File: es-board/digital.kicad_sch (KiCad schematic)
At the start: 25 parts, among them J1 Conn_02x02_Odd_Even, Q5 IRF530NSTRLPB, SW1 SW_SPST, SW2 SW_SPST, SW3 SW_SPST, SW4 SW_SPST, SW5 SW_SPST, U2 ATmega32U4-A, U5 OLED, Y1 16MHz Crystal

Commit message: Added BOM
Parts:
- C1, C4, C5: DPN (none) -> 1276-3091-1-ND; MPN (none) -> CL31B105KBHNFNE
- C2, C3: value 18p -> 24p; DPN (none) -> 478-12061A240JAT2ACT-ND; MPN (none) -> 12061A240JAT2A
- C6, C7: DPN (none) -> 1276-1017-1-ND; MPN (none) -> CL31B104KBCNNNC
- D1: DPN (none) -> 160-1169-1-ND; MPN (none) -> LTST-C150GKT
- D2: DPN (none) -> 160-1403-1-ND; MPN (none) -> LTST-C150KFKT
- J1: value Conn_02x02_Odd_Even -> DNP
- R1: DPN (none) -> RMCF1206JG100K; MPN (none) -> RMCF1206JG100K
- R14, R6: DPN (none) -> 738-RMCF1206JG10K0CT-ND; MPN (none) -> RMCF1206JG10K0
- R7, R8: DPN (none) -> RMCF1206JT1K00CT-ND; MPN (none) -> RMCF1206JT1K00
- SW1, SW2, SW3, SW4, SW5: footprint Button_Switch_SMD:SW_Push_1P1T_NO_6x6mm_H9.5mm -> Button_Switch_SMD:SW_SPST_SKQG_WithStem; DPN (none) -> CKN12220-1-ND; MPN (none) -> PTS526 SM15 SMTR2 LFS
- U2: DPN (none) -> ATMEGA32U4-AURCT-ND; MPN (none) -> IC MCU 8BIT 32KB FLASH 44TQFP
- U5: DPN (none) -> 1528-1512-ND; MPN (none) -> 938
- Y1: DPN (none) -> 2151-RH100-16.000-16-3030-EXT-TRCT-ND; MPN (none) -> RH100-16.000-16-3030-EXT-TR
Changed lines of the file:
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@@
+      (effects (font (size 1.27 1.27)) hide)
+    )
+    (property "DPN" "2151-RH100-16.000-16-3030-EXT-TRCT-ND" (at 47.625 66.04 0)
+      (effects (font (size 1.27 1.27)) hide)
+    )
+    (property "MPN" "RH100-16.000-16-3030-EXT-TR" (at 47.625 66.04 0)
       (effects (font (size 1.27 1.27)) hide)
     )
@@
       (effects (font (size 1.27 1.27)) hide)
     )
+    (property "DPN" "160-1169-1-ND" (at 34.925 129.54 0)
+      (effects (font (size 1.27 1.27)) hide)
+    )
+    (property "MPN" "LTST-C150GKT" (at 34.925 129.54 0)
+      (effects (font (size 1.27 1.27)) hide)
+    )
     (pin "1")
     (pin "2")
@@
       (effects (font (size 1.27 1.27)))
     )
-    (property "Value" "18p" (at 34.925 66.04 90)
+    (property "Value" "24p" (at 34.925 66.04 90)
       (effects (font (size 1.27 1.27)))
     )
@@
       (effects (font (size 1.27 1.27)) hide)
     )
+    (property "DPN" "478-12061A240JAT2ACT-ND" (at 34.925 69.85 0)
+      (effects (font (size 1.27 1.27)) hide)
+    )
+    (property "MPN" "12061A240JAT2A" (at 34.925 69.85 0)
+      (effects (font (size 1.27 1.27)) hide)
+    )
     (pin "1")
     (pin "2")
@@
       (effects (font (size 1.27 1.27)))
     )
-    (property "Footprint" "Button_Switch_SMD:SW_Push_1P1T_NO_6x6mm_H9.5mm" (at 226.06 109.22 0)
+    (property "Footprint" "Button_Switch_SMD:SW_SPST_SKQG_WithStem" (at 226.06 109.22 0)
       (effects (font (size 1.27 1.27)) hide)
     )
     (property "Datasheet" "~" (at 226.06 109.22 0)
+      (effects (font (size 1.27 1.27)) hide)
+    )
+    (property "DPN" "CKN12220-1-ND" (at 226.06 109.22 0)
+      (effects (font (size 1.27 1.27)) hide)
+    )
+    (property "MPN" "PTS526 SM15 SMTR2 LFS" (at 226.06 109.22 0)
       (effects (font (size 1.27 1.27)) hide)
     )
@@
       (effects (font (size 1.27 1.27)))
     )
-    (property "Footprint" "Button_Switch_SMD:SW_Push_1P1T_NO_6x6mm_H9.5mm" (at 45.085 58.42 0)
+    (property "Footprint" "Button_Switch_SMD:SW_SPST_SKQG_WithStem" (at 45.085 58.42 0)
       (effects (font (size 1.27 1.27)) hide)
     )
@@
       (effects (font (size 1.27 1.27)) hide)
     )
+    (property "DPN" "CKN12220-1-ND" (at 45.085 58.42 0)
+      (effects (font (size 1.27 1.27)) hide)
+    )
+    (property "MPN" "PTS526 SM15 SMTR2 LFS" (at 45.085 58.42 0)
+      (effects (font (size 1.27 1.27)) hide)
+    )
     (pin "1")
     (pin "2")
@@
     )
     (property "Datasheet" "~" (at 31.115 96.52 0)
+      (effects (font (size 1.27 1.27)) hide)
+    )
+    (property "DPN" "1276-1017-1-ND" (at 31.115 96.52 0)
+      (effects (font (size 1.27 1.27)) hide)
+    )
+    (property "MPN" "CL31B104KBCNNNC" (at 31.115 96.52 0)
       (effects (font (size 1.27 1.27)) hide)
     )
@@
     )
     (property "Datasheet" "~" (at 213.995 66.675 0)
+      (effects (font (size 1.27 1.27)) hide)
+    )
+    (property "DPN" "738-RMCF1206JG10K0CT-ND" (at 213.995 66.675 0)
+      (effects (font (size 1.27 1.27)) hide)
+    )
+    (property "MPN" "RMCF1206JG10K0" (at 213.995 66.675 0)
       (effects (font (size 1.27 1.27)) hide)
     )
@@
       (effects (font (size 1.27 1.27)) hide)
     )
+    (property "DPN" "RMCF1206JG100K" (at 61.595 54.61 0)
+      (effects (font (size 1.27 1.27)) hide)
+    )
+    (property "MPN" "RMCF1206JG100K" (at 61.595 54.61 0)
+      (effects (font (size 1.27 1.27)) hide)
+    )
     (pin "1")
     (pin "2")
@@
       (effects (font (size 1.27 1.27)) hide)
     )
+    (property "DPN" "1276-3091-1-ND" (at 53.975 54.61 0)
+      (effects (font (size 1.27 1.27)) hide)
+    )
+    (property "MPN" "CL31B105KBHNFNE" (at 53.975 54.61 0)
+      (effects (font (size 1.27 1.27)) hide)
+    )
     (pin "1")
     (pin "2")
@@
       (effects (font (size 1.27 1.27)))
     )
-    (property "Footprint" "Button_Switch_SMD:SW_Push_1P1T_NO_6x6mm_H9.5mm" (at 226.06 116.84 0)
+    (property "Footprint" "Button_Switch_SMD:SW_SPST_SKQG_WithStem" (at 226.06 116.84 0)
       (effects (font (size 1.27 1.27)) hide)
     )
     (property "Datasheet" "~" (at 226.06 116.84 0)
+      (effects (font (size 1.27 1.27)) hide)
+    )
+    (property "DPN" "CKN12220-1-ND" (at 226.06 116.84 0)
+      (effects (font (size 1.27 1.27)) hide)
+    )
+    (property "MPN" "PTS526 SM15 SMTR2 LFS" (at 226.06 116.84 0)
       (effects (font (size 1.27 1.27)) hide)
     )
@@
     )
     (property "Datasheet" "http://ww1.microchip.com/downloads/en/DeviceDoc/Atmel-7766-8-bit-AVR-ATmega16U4-32U4_Datasheet.pdf" (at 85.725 96.52 0)
+      (effects (font (size 1.27 1.27)) hide)
+    )
+    (property "DPN" "ATMEGA32U4-AURCT-ND" (at 85.725 96.52 0)
+      (effects (font (size 1.27 1.27)) hide)
+    )
+    (property "MPN" "IC MCU 8BIT 32KB FLASH 44TQFP" (at 85.725 96.52 0)
       (effects (font (size 1.27 1.27)) hide)
     )
@@
       (effects (font (size 1.27 1.27)) hide)
     )
+    (property "DPN" "1276-3091-1-ND" (at 60.325 99.06 0)
+      (effects (font (size 1.27 1.27)) hide)
+    )
+    (property "MPN" "CL31B105KBHNFNE" (at 60.325 99.06 0)
+      (effects (font (size 1.27 1.27)) hide)
+    )
     (pin "1")
     (pin "2")
@@
       (effects (font (size 1.27 1.27)) hide)
     )
+    (property "DPN" "160-1403-1-ND" (at 50.165 139.7 0)
+      (effects (font (size 1.27 1.27)) hide)
+    )
+    (property "MPN" "LTST-C150KFKT" (at 50.165 139.7 0)
+      (effects (font (size 1.27 1.27)) hide)
+    )
     (pin "1")
     (pin "2")
@@
       (effects (font (size 1.27 1.27)))
     )
-    (property "Footprint" "Button_Switch_SMD:SW_Push_1P1T_NO_6x6mm_H9.5mm" (at 226.06 101.6 0)
+    (property "Footprint" "Button_Switch_SMD:SW_SPST_SKQG_WithStem" (at 226.06 101.6 0)
       (effects (font (size 1.27 1.27)) hide)
     )
@@
       (effects (font (size 1.27 1.27)) hide)
     )
+    (property "DPN" "CKN12220-1-ND" (at 226.06 101.6 0)
+      (effects (font (size 1.27 1.27)) hide)
+    )
+    (property "MPN" "PTS526 SM15 SMTR2 LFS" (at 226.06 101.6 0)
+      (effects (font (size 1.27 1.27)) hide)
+    )
     (pin "1")
     (pin "2")
@@
       (effects (font (size 1.27 1.27)))
     )
-    (property "Value" "18p" (at 34.925 58.42 90)
+    (property "Value" "24p" (at 34.925 58.42 90)
       (effects (font (size 1.27 1.27)))
     )
@@
       (effects (font (size 1.27 1.27)) hide)
     )
+    (property "DPN" "478-12061A240JAT2ACT-ND" (at 34.925 62.23 0)
+      (effects (font (size 1.27 1.27)) hide)
+    )
+    (property "MPN" "12061A240JAT2A" (at 34.925 62.23 0)
+      (effects (font (size 1.27 1.27)) hide)
+    )
     (pin "1")
     (pin "2")
@@
     )
     (property "Datasheet" "~" (at 50.165 129.54 0)
+      (effects (font (size 1.27 1.27)) hide)
+    )
+    (property "DPN" "RMCF1206JT1K00CT-ND" (at 50.165 129.54 0)
+      (effects (font (size 1.27 1.27)) hide)
+    )
+    (property "MPN" "RMCF1206JT1K00" (at 50.165 129.54 0)
       (effects (font (size 1.27 1.27)) hide)
     )
@@
       (effects (font (size 1.27 1.27)))
     )
-    (property "Value" "Conn_02x02_Odd_Even" (at 64.135 153.67 0)
+    (property "Value" "DNP" (at 64.135 153.67 0)
       (effects (font (size 1.27 1.27)))
     )
@@
       (effects (font (size 1.27 1.27)) hide)
     )
+    (property "DPN" "1276-1017-1-ND" (at 43.815 96.52 0)
+      (effects (font (size 1.27 1.27)) hide)
+    )
+    (property "MPN" "CL31B104KBCNNNC" (at 43.815 96.52 0)
+      (effects (font (size 1.27 1.27)) hide)
+    )
     (pin "1")
     (pin "2")
@@
       (effects (font (size 1.27 1.27)) hide)
     )
-    (property "Sim.Device" "NMOS" (at 219.075 76.835 0)
-      (effects (font (size 1.27 1.27)) hide)
-    )
-    (property "Sim.Type" "VDMOS" (at 219.075 78.74 0)
-      (effects (font (size 1.27 1.27)) hide)
-    )
-    (property "Sim.Pins" "1=D 2=G 3=S" (at 219.075 74.93 0)
-      (effects (font (size 1.27 1.27)) hide)
-    )
     (property "DPN" "IRF530NSTRLPBFCT-ND" (at 219.075 59.69 0)
       (effects (font (size 1.27 1.27)) hide)
@@
       (effects (font (size 1.27 1.27)) hide)
     )
+    (property "DPN" "738-RMCF1206JG10K0CT-ND" (at 121.285 118.11 0)
+      (effects (font (size 1.27 1.27)) hide)
+    )
+    (property "MPN" "RMCF1206JG10K0" (at 121.285 118.11 0)
+      (effects (font (size 1.27 1.27)) hide)
+    )
     (pin "1")
     (pin "2")
@@
       (effects (font (size 1.27 1.27)) hide)
     )
+    (property "DPN" "RMCF1206JT1K00CT-ND" (at 34.925 139.7 0)
+      (effects (font (size 1.27 1.27)) hide)
+    )
+    (property "MPN" "RMCF1206JT1K00" (at 34.925 139.7 0)
+      (effects (font (size 1.27 1.27)) hide)
+    )
     (pin "1")
     (pin "2")
@@
       (effects (font (size 1.27 1.27)))
     )
-    (property "Footprint" "Button_Switch_SMD:SW_Push_1P1T_NO_6x6mm_H9.5mm" (at 226.06 124.46 0)
+    (property "Footprint" "Button_Switch_SMD:SW_SPST_SKQG_WithStem" (at 226.06 124.46 0)
       (effects (font (size 1.27 1.27)) hide)
     )
     (property "Datasheet" "~" (at 226.06 124.46 0)
+      (effects (font (size 1.27 1.27)) hide)
+    )
+    (property "DPN" "CKN12220-1-ND" (at 226.06 124.46 0)
+      (effects (font (size 1.27 1.27)) hide)
+    )
+    (property "MPN" "PTS526 SM15 SMTR2 LFS" (at 226.06 124.46 0)
       (effects (font (size 1.27 1.27)) hide)
     )
@@
       (effects (font (size 1.27 1.27)) hide)
     )
+    (property "DPN" "1276-3091-1-ND" (at 56.515 73.66 0)
+      (effects (font (size 1.27 1.27)) hide)
+    )
+    (property "MPN" "CL31B105KBHNFNE" (at 56.515 73.66 0)
+      (effects (font (size 1.27 1.27)) hide)
+    )
     (pin "1")
     (pin "2")
@@
       (effects (font (size 1.27 1.27)) hide)
     )
+    (property "DPN" "1528-1512-ND" (at 173.99 136.525 0)
+      (effects (font (size 1.27 1.27)) hide)
+    )
+    (property "MPN" "938" (at 173.99 136.525 0)
+      (effects (font (size 1.27 1.27)) hide)
+    )

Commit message: Finished electricaling
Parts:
- removed C15: value to boom, Connector_PinHeader_2.54mm:PinHeader_1x02_P2.54mm_Vertical, symbol Device:C
- added J2: Conn_01x04, Connector_PinHeader_2.54mm:PinHeader_1x04_P2.54mm_Vertical, symbol Connector_Generic:Conn_01x04
- added R15, R16: 0, Resistor_SMD:R_1206_3216Metric, symbol Device:R
- added TP1, TP2: TestPoint, Connector_PinHeader_1.00mm:PinHeader_1x01_P1.00mm_Vertical, symbol Connector:TestPoint
- added TP3: Conn_01x02, Connector_PinHeader_2.54mm:PinHeader_1x02_P2.54mm_Vertical, symbol Connector_Generic:Conn_01x02
- J1: footprint Connector_PinHeader_2.54mm:PinHeader_1x04_P2.54mm_Vertical -> Connector_PinHeader_2.54mm:PinHeader_2x03_P2.54mm_Vertical; symbol Connector_Generic:Conn_02x02_Odd_Even -> Connector_Generic:Conn_02x03_Odd_Even
- SW1, SW2, SW3, SW4, SW5: footprint Button_Switch_SMD:SW_SPST_SKQG_WithStem -> explosnake:SW_SPST_SKQG_WithStem
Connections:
- net io10 - DOWN is gone; now on net btnDOWN: SW3.1 (A)
- net io11 is gone; now on net USB_PD_FAULT: U2.12 (PB7)
- net io11 - LEFT is gone; now on net btnLEFT: SW4.1 (A)
- net io12 - RIGHT is gone; now on net btnRIGHT: SW5.1 (A)
- net +5V: now also J1.2 (Pin_2), J2.2 (Pin_2)
- net GND: now also J1.6 (Pin_6), J2.4 (Pin_4)
- net Reset: now also J1.5 (Pin_5)
- net VBUS: now also J2.1 (Pin_1)
- net miso: now also J1.1 (Pin_1)
- net mosi: now also J1.4 (Pin_4)
- net rxled: now also TP1.1
- net sck: now also J1.3 (Pin_3)
- net txled: now also TP2.1
- net at Q5.2 (D): now also J2.3 (Pin_3)
- net a0: no longer names the net of U2.36 (PF7)
- net a0: no longer U5.4 (SDA)
- net a1: no longer names the net of U2.37 (PF6)
- net a1: no longer U5.3 (SCL)
- net a2: no longer names the net of U2.38 (PF5)
- net a3: no longer names the net of U2.39 (PF4)
- net a4: no longer names the net of U2.40 (PF1)
- net a5: no longer names the net of U2.41 (PF0)
- net d0/rx renamed rx
- net rx: now also TP3.1 (Pin_1); no longer J1.3 (Pin_3)
- net d1/tx renamed tx
- net tx: now also TP3.2 (Pin_2); no longer J1.1 (Pin_1)
- net d2/sda: no longer names the net of U2.19 (PD1)
- net d2/sda: now also R16.1; no longer J1.4 (Pin_4)
- net d3/scl: no longer names the net of U2.18 (PD0)
- net d3/scl: now also R15.1; no longer J1.2 (Pin_2)
- net d4: no longer names the net of U2.25 (PD4)
- net d5: no longer names the net of U2.31 (PC6)
- net d6 renamed btnLEFT
- net d7: no longer names the net of U2.1 (PE6)
- net io10 renamed btnDOWN
- net io12 renamed btnRIGHT
- net io8 renamed capboom
- net capboom: now also Q5.1 (G), R14.2
- net io8 - UP renamed btnUP
- net btnUP: now also U2.29 (PB5)
- removed net io9: Q5.1 (G), R14.2, U2.29 (PB5)
- new net scl: R15.2, U5.3 (SCL)
- new net sda: R16.2, U5.4 (SDA)
- no-connect marks 0 -> 9
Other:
- note added: "a0"
- note added: "a1"
- note added: "a2"
- note added: "a3"
- note added: "a4"
- note added: "a5"
- note added: "d0"
- note added: "d1"
- note added: "d10"
- note added: "d11"
- note added: "d12"
- note added: "d13"
- note added: "d15"
- note added: "d16"
- note added: "d17"
- note added: "d2"
- note added: "d3"
- note added: "d4"
- note added: "d5"
- note added: "d6"
- note added: "d7"
- note added: "d8"
- note added: "d9"
- note removed: "TODO - Connect this to a digital input so that we can alert the user that their power brick can't run the device. USB_PD_FAULT goes high when there is a fault"
- moved on the sheet: C1, C2, C3, C4, C5, C6, C7, D1, D2, Q5, R1, R14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

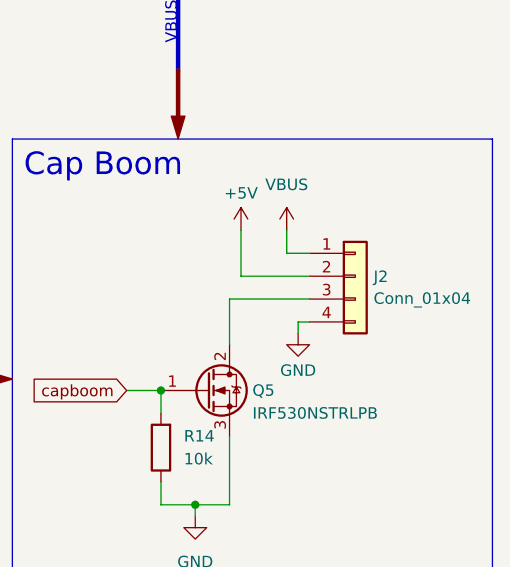
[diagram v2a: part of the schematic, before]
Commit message: Fixed board outline and silkscreen
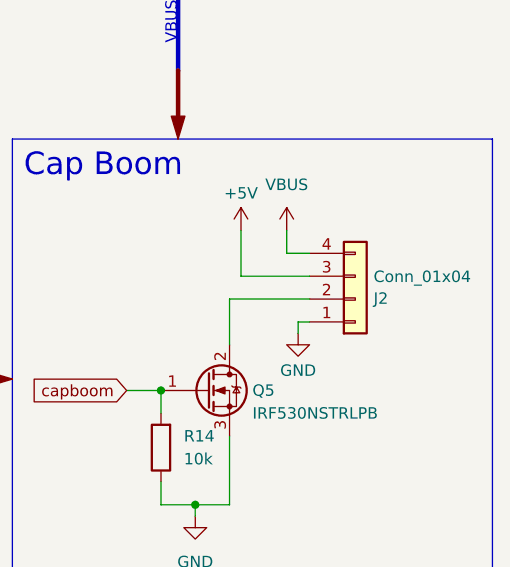
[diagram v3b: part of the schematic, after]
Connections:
- net +5V: now also J2.3 (Pin_3); no longer J2.2 (Pin_2)
- net GND: now also J2.1 (Pin_1); no longer J2.4 (Pin_4)
- net VBUS: now also J2.4 (Pin_4); no longer J2.1 (Pin_1)
- net at Q5.2 (D): now also J2.2 (Pin_2); no longer J2.3 (Pin_3)
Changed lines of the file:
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@@
     )
   )
-  (symbol (lib_id "Connector_Generic:Conn_01x04") (at 236.22 46.99 0) (unit 1)
-    (in_bom yes) (on_board yes) (dnp no) (fields_autoplaced)
-    (property "Reference" "J2" (at 238.252 47.0479 0)
+  (symbol (lib_id "Connector_Generic:Conn_01x04") (at 236.22 49.53 0) (mirror x) (unit 1)
+    (in_bom yes) (on_board yes) (dnp no)
+    (property "Reference" "J2" (at 238.252 49.4721 0)
       (effects (font (size 1.27 1.27)) (justify left))
     )
-    (property "Value" "Conn_01x04" (at 238.252 49.4721 0)
+    (property "Value" "Conn_01x04" (at 238.252 47.0479 0)
       (effects (font (size 1.27 1.27)) (justify left))
     )
-    (property "Footprint" "Connector_PinHeader_2.54mm:PinHeader_1x04_P2.54mm_Vertical" (at 236.22 46.99 0)
+    (property "Footprint" "Connector_PinHeader_2.54mm:PinHeader_1x04_P2.54mm_Vertical" (at 236.22 49.53 0)
       (effects (font (size 1.27 1.27)) hide)
     )
-    (property "Datasheet" "~" (at 236.22 46.99 0)
+    (property "Datasheet" "~" (at 236.22 49.53 0)
       (effects (font (size 1.27 1.27)) hide)
     )
